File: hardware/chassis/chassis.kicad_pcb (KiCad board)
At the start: 2 copper layers, 60.3 x 52.7 mm, 108 parts, among them J1 RJ45_LED_Shielded, Q1 SiR422DP, Q2 Si7898DP, Q3 MMDT3906, T1 PoE_Transformer, T2 Pulse_Transformer, U1 TPS23754PWPR, U2 TCMT1107, U3 TCMT1107, U4 KSZ8081RND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

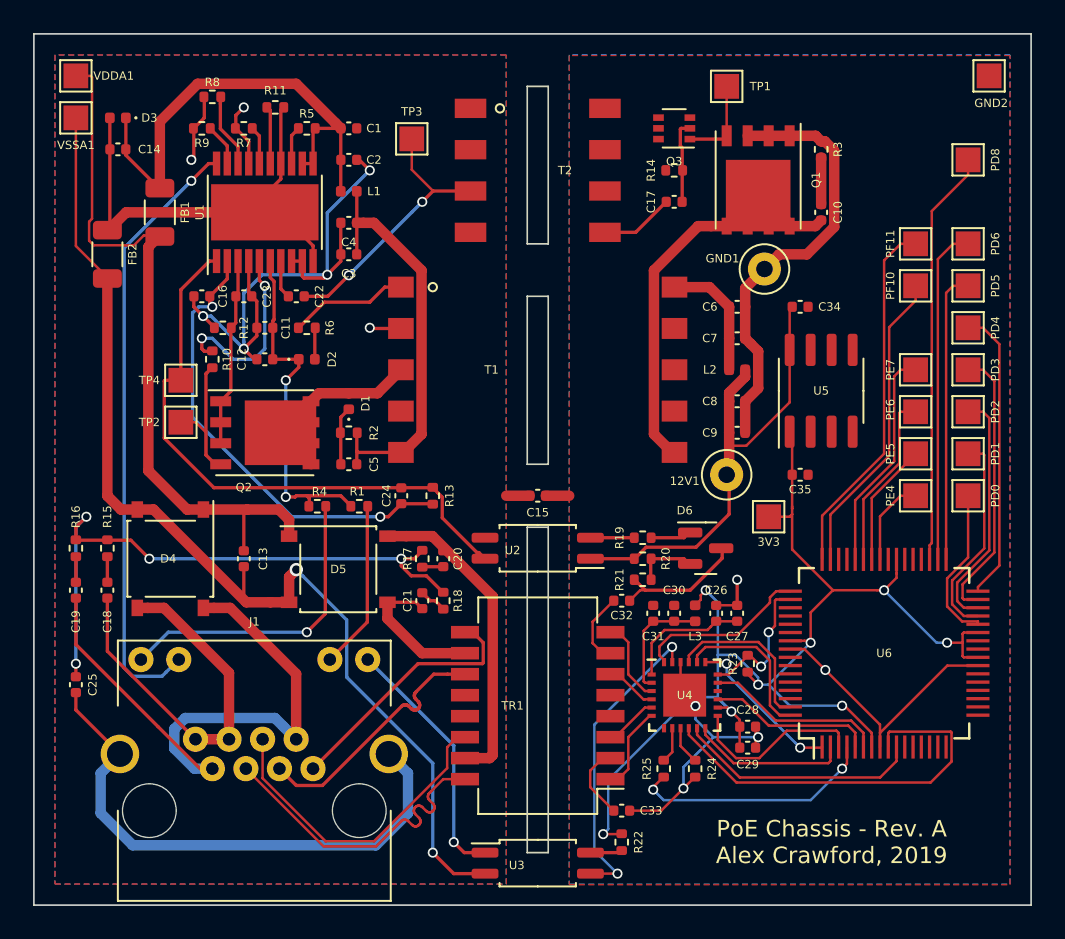
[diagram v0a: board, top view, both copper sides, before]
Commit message: hardware: prepare for more KiCad projects
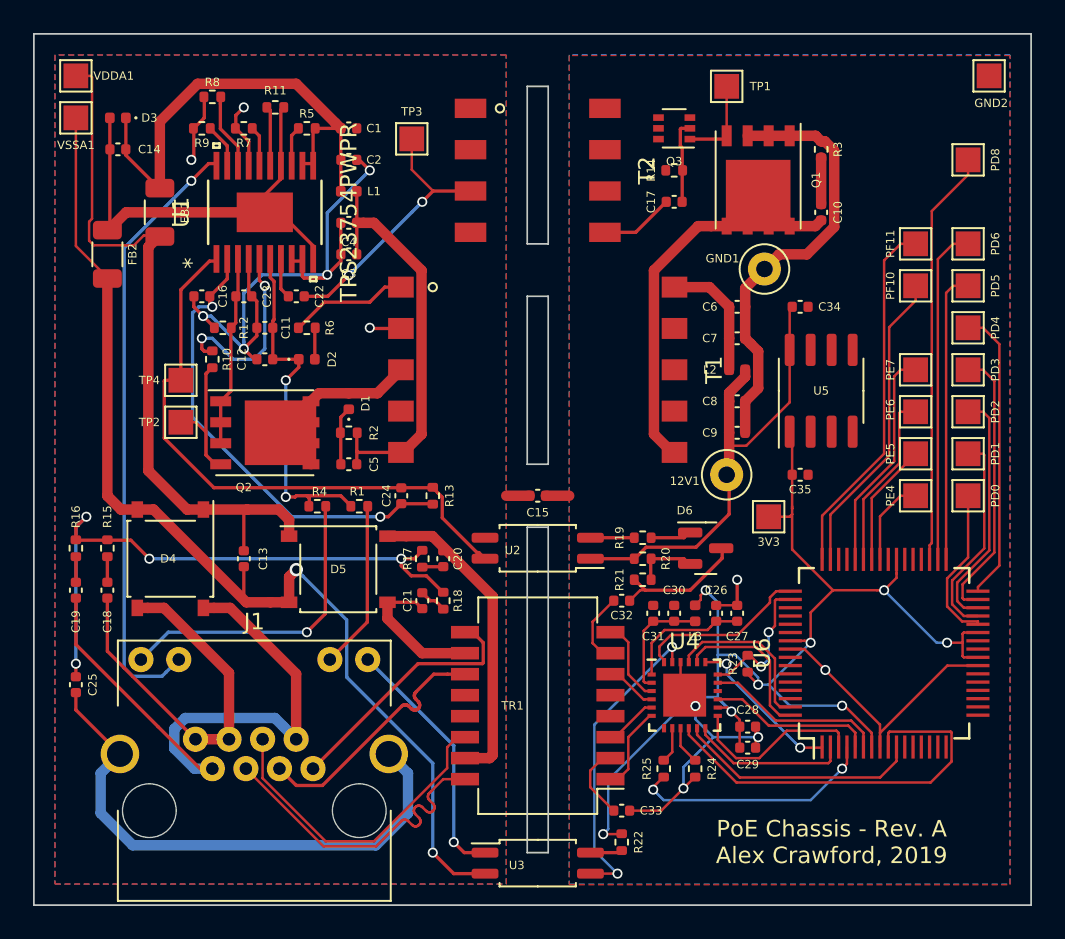
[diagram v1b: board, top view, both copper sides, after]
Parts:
- J1: footprint chassis:RJHSE-538X -> common:RJHSE-538X
- T1: footprint chassis:POE_EP13 -> common:POE_EP13
- T2: footprint chassis:GDTI_EP7 -> common:GDTI_EP7
- U1: footprint Package_SO:HTSSOP-20-1EP_4.4x6.5mm_P0.65mm_EP3.4x6.5mm -> common:TSSOP-20
- U4: footprint chassis:QFN-24 -> common:QFN-24
- U6: footprint chassis:QFP-64 -> common:QFP-64
